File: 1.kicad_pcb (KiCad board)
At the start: 2 copper layers, 55.9 x 35.6 mm, 24 parts, among them J1 Screw_Terminal_01x03, J2 Screw_Terminal_01x01, J3 Screw_Terminal_01x01, U1 LTC2990, U2 LTC2990, U3 LTC2990

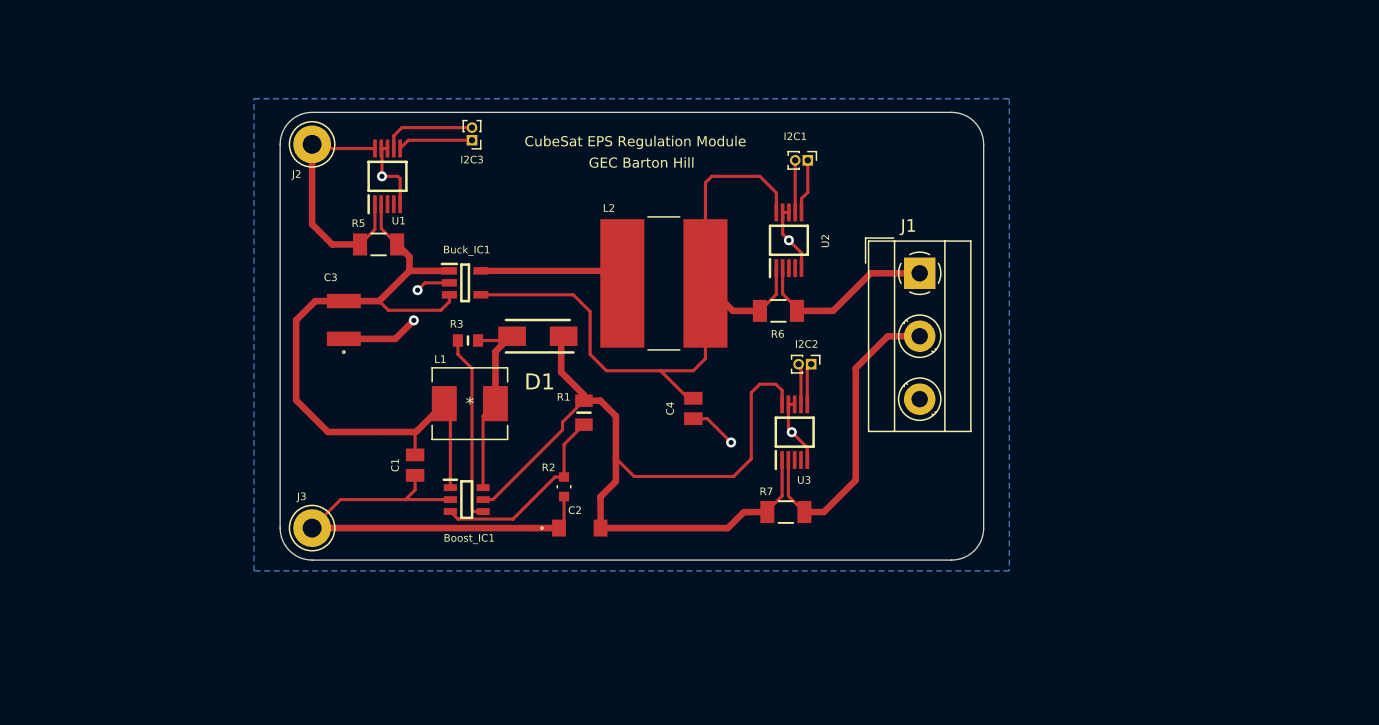
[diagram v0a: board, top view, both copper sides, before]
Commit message: Start redesign coz boost circuit is f'd up
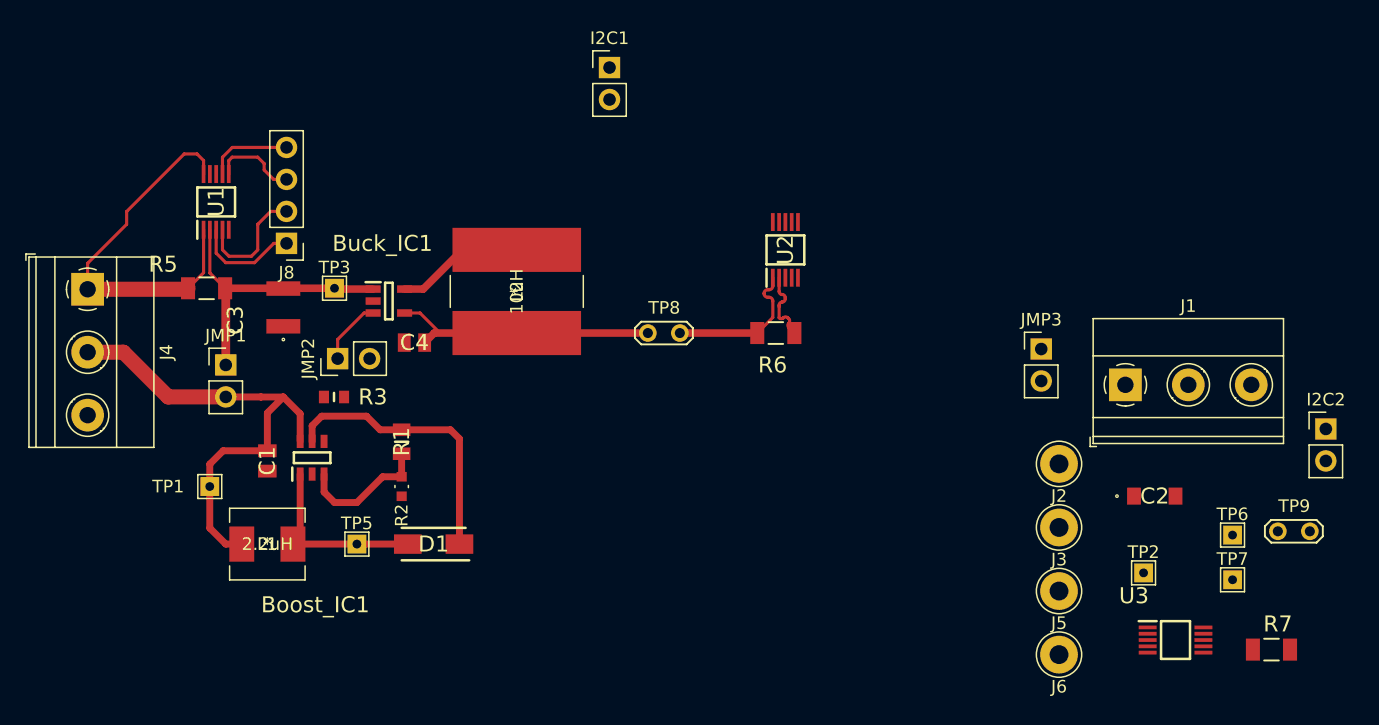
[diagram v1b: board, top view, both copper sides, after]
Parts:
- removed I2C3: EN, Connector_PinHeader_1.00mm:PinHeader_1x02_P1.00mm_Vertical
- added J4: Conn_01x03_Pin, TerminalBlock_Phoenix:TerminalBlock_Phoenix_MKDS-1,5-3_1x03_P5.00mm_Horizontal, F.Cu at (116.8, 82.6)
- added J5: Screw_Terminal_01x01, Connector_Pin:Pin_D1.3mm_L11.0mm_LooseFit, F.Cu at (193.9, 106.6)
- added J6: Screw_Terminal_01x01, Connector_Pin:Pin_D1.3mm_L11.0mm_LooseFit, F.Cu at (193.9, 111.6)
- added J8: Conn_01x04_Pin, Connector_PinHeader_2.54mm:PinHeader_1x04_P2.54mm_Vertical, F.Cu at (132.6, 79.0)
- added JMP1: EN, Connector_PinHeader_2.54mm:PinHeader_1x02_P2.54mm_Vertical, F.Cu at (127.8, 88.6)
- added JMP2: EN, Connector_PinHeader_2.54mm:PinHeader_1x02_P2.54mm_Vertical, F.Cu at (136.6, 88.1)
- added JMP3: EN, Connector_PinHeader_2.54mm:PinHeader_1x02_P2.54mm_Vertical, F.Cu at (192.5, 87.4)
- added TP1: TestPoint, TestPoint:TestPoint_THTPad_1.5x1.5mm_Drill0.7mm, F.Cu at (126.5, 98.3)
- added TP2: TestPoint, TestPoint:TestPoint_THTPad_1.5x1.5mm_Drill0.7mm, F.Cu at (200.7, 105.2)
- added TP3: TestPoint, TestPoint:TestPoint_THTPad_1.5x1.5mm_Drill0.7mm, F.Cu at (136.4, 82.5)
- added TP5: TestPoint, TestPoint:TestPoint_THTPad_1.5x1.5mm_Drill0.7mm, F.Cu at (138.2, 102.9)
- added TP6: TestPoint, TestPoint:TestPoint_THTPad_1.5x1.5mm_Drill0.7mm, F.Cu at (207.7, 102.2)
- added TP7: TestPoint, TestPoint:TestPoint_THTPad_1.5x1.5mm_Drill0.7mm, F.Cu at (207.7, 105.7)
- added TP8: TestPoint_2Pole, TestPoint:TestPoint_2Pads_Pitch2.54mm_Drill0.8mm, F.Cu at (161.3, 86.1)
- added TP9: TestPoint_2Pole, TestPoint:TestPoint_2Pads_Pitch2.54mm_Drill0.8mm, F.Cu at (211.3, 101.9)
- D1: value D_Schottky -> STPS2150A
- I2C1, I2C2: footprint Connector_PinHeader_1.00mm:PinHeader_1x02_P1.00mm_Vertical -> Connector_PinHeader_2.54mm:PinHeader_1x02_P2.54mm_Vertical
- J1: footprint TerminalBlock_MetzConnect:TerminalBlock_MetzConnect_Type055_RT01503HDWU_1x03_P5.00mm_Horizontal -> TerminalBlock_Phoenix:TerminalBlock_Phoenix_MKDS-1,5-3_1x03_P5.00mm_Horizontal
- moved J2 64.5 mm to (193.9, 96.5)
- moved J3 59.3 mm to (193.9, 101.5)
- moved C2 45.7 mm to (201.5, 99.1)
- moved I2C2 41.2 mm to (215.1, 93.7), turned to 0 degrees
- moved R7 40.1 mm to (210.8, 111.3)
- moved U3 34.5 mm to (203.2, 110.5), turned to 0 degrees
- moved C4 22.8 mm to (142.7, 86.9), turned to 180 degrees
- moved L1 19.6 mm to (131.1, 102.9)
- moved J1 18.6 mm to (199.2, 90.2), turned to 0 degrees
- moved D1 18.5 mm to (144.3, 102.9)
- moved I2C1 17.4 mm to (158.2, 65.0), turned to 0 degrees
- moved R1 14.7 mm to (141.7, 94.7)
- moved R5 14.1 mm to (126.2, 82.5)
- moved U1 13.8 mm to (127.0, 75.7)
- moved R2 12.9 mm to (141.7, 98.3)
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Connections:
- Boost_IC1 pad 1: Net-(Boost_IC1-Pad1) -> Net-(Boost_IC1-SW)
- Boost_IC1 pad 5: Net-(Boost_IC1-Pad5) -> Net-(Boost_IC1-VOUT)
- Boost_IC1 pad 6: Net-(Boost_IC1-Pad6) -> Net-(Boost_IC1-VIN)
- Buck_IC1 pad 1: Net-(Boost_IC1-Pad1) -> Net-(Buck_IC1-VI)
- Buck_IC1 pad 3: Net-(Boost_IC1-Pad1) -> Net-(Buck_IC1-EN)
- Buck_IC1 pad 4: Net-(Buck_IC1-Pad4) -> Net-(Buck_IC1-FB)
- C1 pad 1: Net-(Boost_IC1-Pad1) -> Net-(Boost_IC1-VIN)
- C2 pad 2: Net-(Boost_IC1-Pad5) -> Net-(Boost_IC1-VOUT)
- C3 pad 2: Net-(Boost_IC1-Pad1) -> Net-(Buck_IC1-VI)
- C4 pad 1: Net-(Buck_IC1-Pad4) -> Net-(Buck_IC1-FB)
- D1 pad 1: Net-(Boost_IC1-Pad5) -> Net-(Boost_IC1-VOUT)
- D1 pad 2: Net-(Boost_IC1-Pad6) -> Net-(Boost_IC1-SW)
- J2 pad 1: Net-(J2-Pad1) -> Earth
- L1 pad 1: Net-(Boost_IC1-Pad1) -> Net-(Boost_IC1-VIN)
- L1 pad 2: Net-(Boost_IC1-Pad6) -> Net-(Boost_IC1-SW)
- L2 pad 2: Net-(Buck_IC1-Pad4) -> Net-(Buck_IC1-FB)
- R1 pad 2: Net-(Boost_IC1-Pad5) -> Net-(Boost_IC1-VOUT)
- R3 pad 2: Net-(Boost_IC1-Pad6) -> Net-(JMP2-Pin_2)
- R5 pad 1: Net-(J2-Pad1) -> Net-(J4-Pin_1)
- R5 pad 2: Net-(Boost_IC1-Pad1) -> Net-(Buck_IC1-VI)
- R6 pad 1: Net-(Buck_IC1-Pad4) -> Net-(U2-V1)
- R7 pad 1: Net-(Boost_IC1-Pad5) -> Net-(U3-V1)
- U1 pad 1: Net-(J2-Pad1) -> Net-(J4-Pin_1)
- U1 pad 10: Net-(J2-Pad1) -> Net-(J4-Pin_1)
- U1 pad 2: Net-(Boost_IC1-Pad1) -> Net-(Buck_IC1-VI)
- U1 pad 3: unconnected-(U1-Pad3) -> Net-(J8-Pin_1)
- U1 pad 4: unconnected-(U1-Pad4) -> Net-(J8-Pin_2)
- U2 pad 1: Net-(Buck_IC1-Pad4) -> Net-(U2-V1)
- U2 pad 10: Net-(Buck_IC1-Pad4) -> Net-(U2-V1)
- U2 pad 3: unconnected-(U2-Pad3) -> Net-(JMP3-Pin_1)
- U2 pad 4: unconnected-(U2-Pad4) -> Net-(JMP3-Pin_2)
- U3 pad 1: Net-(Boost_IC1-Pad5) -> Net-(U3-V1)
- U3 pad 10: Net-(Boost_IC1-Pad5) -> Net-(U3-V1)
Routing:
- net Net-(Boost_IC1-Pad5): track 69.6 -> 0.00 mm
- net Earth: track 66.5 -> 0.00 mm, vias 6 -> 0
- net Net-(Buck_IC1-Pad4): track 57.3 -> 0.00 mm
- net Net-(Boost_IC1-Pad1): track 55.6 -> 0.00 mm
- net Net-(Boost_IC1-VIN): track 0.00 -> 39.1 mm
- net Net-(J4-Pin_1): track 0.00 -> 30.5 mm
- net Net-(Buck_IC1-FB): track 0.00 -> 27.6 mm
- net Net-(J1-Pin_2): track 24.8 -> 0.00 mm
- net Net-(Buck_IC1-VI): track 0.00 -> 23.2 mm
- net Net-(Boost_IC1-VOUT): track 0.00 -> 22.4 mm
- net Net-(J2-Pad1): track 19.6 -> 0.00 mm
- net Net-(Boost_IC1-Pad6): track 15.8 -> 0.00 mm
- net Net-(Boost_IC1-SW): track 0.00 -> 14.9 mm
- net Net-(Boost_IC1-~{SHDN}): track 14.9 -> 0.00 mm
- net Net-(U2-V1): track 0.00 -> 11.9 mm
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- removed copper zone on B.Cu, net Earth
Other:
- board outline removed
- board text removed: "CubeSat EPS Regulation Module"
- board text removed: "GEC Barton Hill"

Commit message: Almost there
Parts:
- removed I2C1, I2C2, JMP2, JMP3: EN, Connector_PinHeader_2.54mm:PinHeader_1x02_P2.54mm_Vertical
- removed R6, R7: 50m, 50m RST:RESC3216X88N
- removed TP2, TP7: TestPoint, TestPoint:TestPoint_THTPad_1.5x1.5mm_Drill0.7mm
- removed U2, U3: LTC2990, MON & PROTECC:SOP50P490X110-10N
- added J7: Conn_01x01_Pin, Connector_PinHeader_2.54mm:PinHeader_1x01_P2.54mm_Vertical, F.Cu at (136.7, 86.4)
- added J9: Conn_01x01_Pin, Connector_PinHeader_2.54mm:PinHeader_1x01_P2.54mm_Vertical, F.Cu at (138.4, 91.7)
- moved J2 87.7 mm to (113.3, 62.0)
- moved J3 81.8 mm to (112.5, 109.2)
- moved TP6 62.4 mm to (151.4, 75.4)
- moved J6 50.7 mm to (195.8, 61.0)
- moved C2 50.7 mm to (150.9, 101.3), turned to -90 degrees
- moved TP9 50.1 mm to (161.3, 99.8), turned to -90 degrees
- moved J1 28.3 mm to (170.9, 89.8), turned to -90 degrees
- moved R3 4.11 mm to (138.4, 94.7), turned to 0 degrees
- turned TP8 to -90 degrees
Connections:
- TP8 pad 2: Net-(U2-V1) -> Net-(J1-Pin_1)
- TP9 pad 1: Net-(U3-V1) -> Net-(J1-Pin_2)
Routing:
- net Earth: track 0.00 -> 45.0 mm
- net Net-(Boost_IC1-VOUT): track 22.4 -> 44.1 mm
- net Net-(J1-Pin_2): track 0.00 -> 13.2 mm
- net Net-(U2-V1): track 11.9 -> 0.00 mm
- net Net-(J1-Pin_1): track 5.92 -> 10.1 mm
- net Net-(Boost_IC1-~{SHDN}): track 0.00 -> 3.64 mm
- net Net-(J9-Pin_1): track 0.00 -> 3.38 mm
- net Net-(J4-Pin_1): track 30.5 -> 28.4 mm
- net Net-(Buck_IC1-EN): track 5.21 -> 3.88 mm
- added copper zone on F.Cu, net Earth
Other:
- board outline added: 120.1 x 67.1 mm

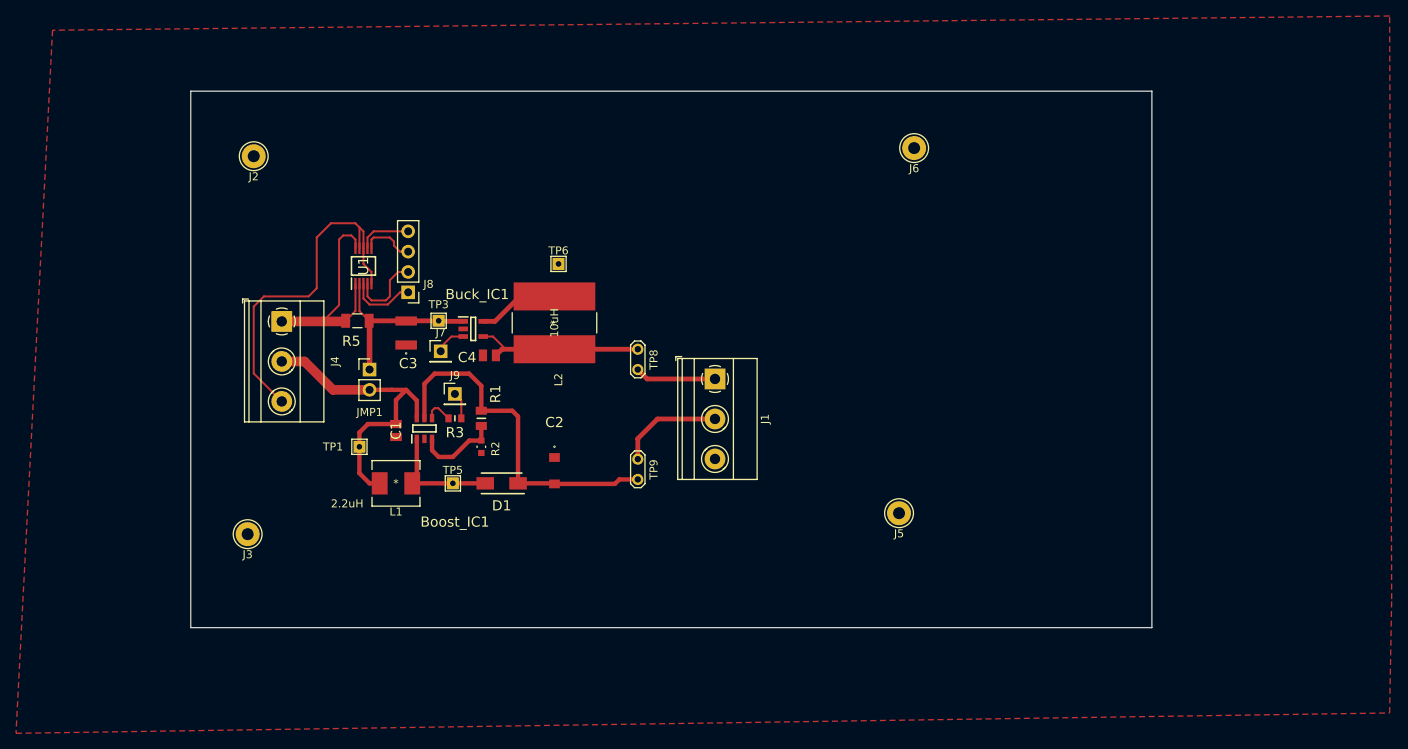
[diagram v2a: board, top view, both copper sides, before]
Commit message: Define edge cuts
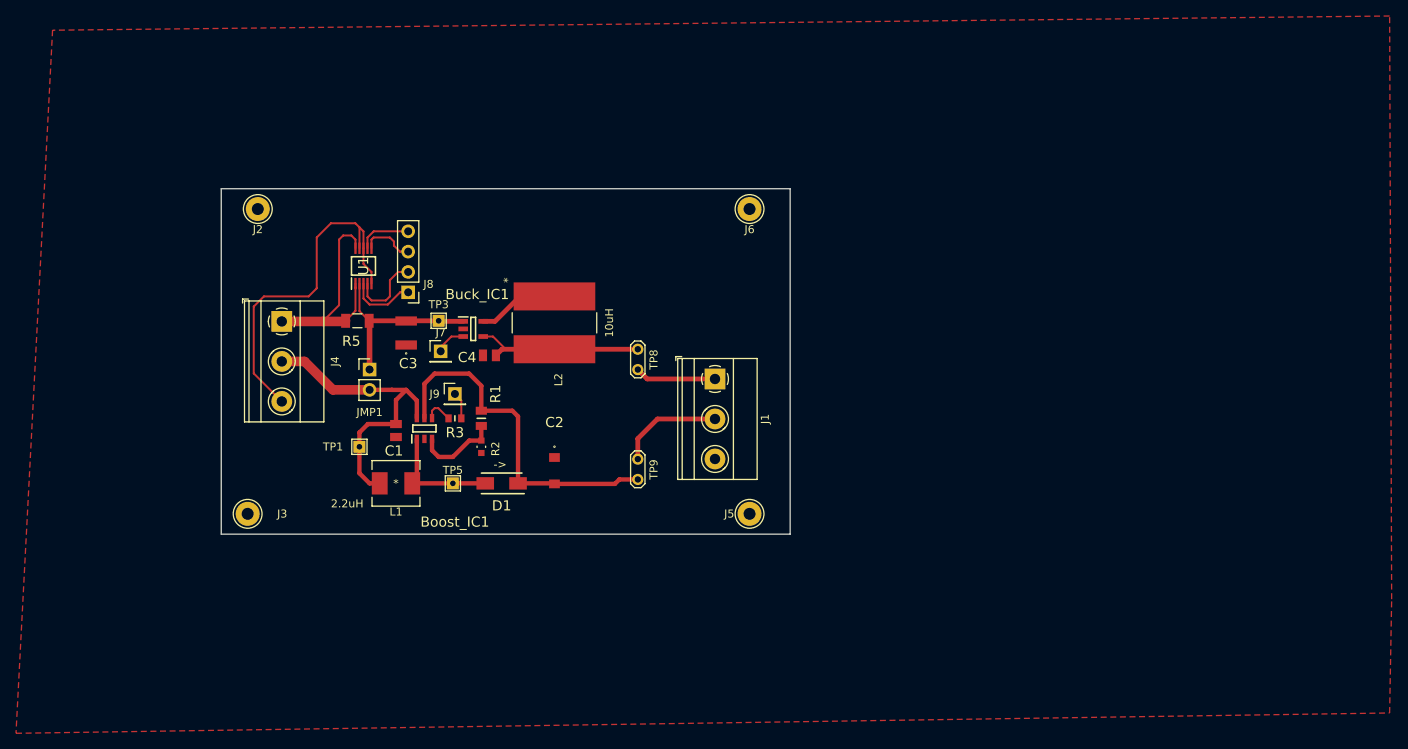
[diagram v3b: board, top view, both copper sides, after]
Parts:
- removed TP6: TestPoint, TestPoint:TestPoint_THTPad_1.5x1.5mm_Drill0.7mm
- moved J6 21.9 mm to (175.3, 68.6)
- moved J5 18.7 mm to (175.3, 106.7)
- moved J2 6.62 mm to (113.8, 68.6)
- moved J3 2.54 mm to (112.5, 106.7)
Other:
- board size 120.1 x 67.1 mm -> 71.1 x 43.2 mm
- board text added: "->"
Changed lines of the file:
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@@
   )
   (footprint "Connector_Pin:Pin_D1.3mm_L11.0mm_LooseFit" (layer "F.Cu")
-    (at 112.522 109.22)
+    (at 112.522 106.68)
     (descr "solder Pin_ diameter 1.3mm, hole diameter 1.5mm (loose fit), length 11.0mm")
     (tags "solder Pin_ loose fit")
@@
     (property "ki_keywords" "screw terminal")
     (attr through_hole)
-    (fp_text reference "J3" (at 0 2.55) (layer "F.SilkS")
+    (fp_text reference "J3" (at 4.318 0) (layer "F.SilkS")
         (effects (font (size 1 1) (thickness 0.15)))
     )
@@
   )
   (footprint "Connector_Pin:Pin_D1.3mm_L11.0mm_LooseFit" (layer "F.Cu")
-    (at 193.946 106.599)
+    (at 175.26 106.68)
     (descr "solder Pin_ diameter 1.3mm, hole diameter 1.5mm (loose fit), length 11.0mm")
     (tags "solder Pin_ loose fit")
@@
     (property "ki_keywords" "screw terminal")
     (attr through_hole)
-    (fp_text reference "J5" (at 0 2.55) (layer "F.SilkS")
+    (fp_text reference "J5" (at -2.54 0) (layer "F.SilkS")
         (effects (font (size 1 1) (thickness 0.15)))
     )
@@
     (property "ki_keywords" "connector")
     (attr through_hole)
-    (fp_text reference "J9" (at 0 -2.33) (layer "F.SilkS")
+    (fp_text reference "J9" (at -2.54 0) (layer "F.SilkS")
         (effects (font (size 1 1) (thickness 0.15)))
     )
@@
       (rotate (xyz 0 0 0))
     )
-  )
-  (footprint "TestPoint:TestPoint_THTPad_1.5x1.5mm_Drill0.7mm" (layer "F.Cu")
-    (at 151.384 75.438)
-    (descr "THT rectangular pad as test Point, square 1.5mm side length, hole diameter 0.7mm")
-    (tags "test point THT pad rectangle square")
-    (property "Sheetfile" "1.kicad_sch")
-    (property "Sheetname" "")
-    (property "ki_description" "test point")
-    (property "ki_keywords" "test point tp")
-    (attr exclude_from_pos_files)
-    (fp_text reference "TP6" (at 0 -1.648) (layer "F.SilkS")
-        (effects (font (size 1 1) (thickness 0.15)))
-    )
-    (fp_text value "TestPoint" (at 0 1.75) (layer "F.Fab")
-        (effects (font (size 1 1) (thickness 0.15)))
-    )
-    (fp_text user "${REFERENCE}" (at 0 -1.65) (layer "F.Fab")
-        (effects (font (size 1 1) (thickness 0.15)))
-    )
-    (fp_line (start -0.95 -0.95) (end 0.95 -0.95)
-      (stroke (width 0.12) (type solid)) (layer "F.SilkS"))
-    (fp_line (start -0.95 0.95) (end -0.95 -0.95)
-      (stroke (width 0.12) (type solid)) (layer "F.SilkS"))
-    (fp_line (start 0.95 -0.95) (end 0.95 0.95)
-      (stroke (width 0.12) (type solid)) (layer "F.SilkS"))
-    (fp_line (start 0.95 0.95) (end -0.95 0.95)
-      (stroke (width 0.12) (type solid)) (layer "F.SilkS"))
-    (fp_line (start -1.25 -1.25) (end -1.25 1.25)
-      (stroke (width 0.05) (type solid)) (layer "F.CrtYd"))
-    (fp_line (start -1.25 -1.25) (end 1.25 -1.25)
-      (stroke (width 0.05) (type solid)) (layer "F.CrtYd"))
-    (fp_line (start 1.25 1.25) (end -1.25 1.25)
-      (stroke (width 0.05) (type solid)) (layer "F.CrtYd"))
-    (fp_line (start 1.25 1.25) (end 1.25 -1.25)
-      (stroke (width 0.05) (type solid)) (layer "F.CrtYd"))
-    (pad "1" thru_hole rect (at 0 0) (size 1.5 1.5) (drill 0.7) (layers "*.Cu" "*.Mask")
-      (net 8 "Net-(Buck_IC1-SW)") (pinfunction "1") (pintype "passive"))
   )
   (footprint "50m RST:RESC3216X88N" (layer "F.Cu")
@@
   )
   (footprint "Connector_Pin:Pin_D1.3mm_L11.0mm_LooseFit" (layer "F.Cu")
-    (at 113.284 61.976)
+    (at 113.792 68.58)
     (descr "solder Pin_ diameter 1.3mm, hole diameter 1.5mm (loose fit), length 11.0mm")
     (tags "solder Pin_ loose fit")
@@
     (property "ki_description" "Cap Aluminum Lytic 10uF 35V 20% (5 X 5.8mm) SMD 0.7 Ohm 160mA 2000h 105C T/R")
     (attr smd)
-    (fp_text reference "C1" (at 0 0 90) (layer "F.SilkS")
+    (fp_text reference "C1" (at 2.54 0.254 -180) (layer "F.SilkS")
         (effects (font (size 1.27 1.27) (thickness 0.254)))
     )
@@
         (effects (font (size 1 1) (thickness 0.15)))
     )
-    (fp_text value "10uH" (at 0 0 90) (layer "F.SilkS")
-        (effects (font (size 1 1) (thickness 0.15)))
-    )
-    (fp_text user "*" (at 0 0 90) (layer "F.SilkS")
+    (fp_text value "10uH" (at 0 -6.858 90) (layer "F.SilkS")
+        (effects (font (size 1 1) (thickness 0.15)))
+    )
+    (fp_text user "*" (at -5.334 5.842 90) (layer "F.SilkS")
         (effects (font (size 1 1) (thickness 0.15)))
     )
@@
   )
   (footprint "Connector_Pin:Pin_D1.3mm_L11.0mm_LooseFit" (layer "F.Cu")
-    (at 195.834 60.96)
+    (at 175.26 68.58)
     (descr "solder Pin_ diameter 1.3mm, hole diameter 1.5mm (loose fit), length 11.0mm")
     (tags "solder Pin_ loose fit")
@@
     )
   )
-  (gr_rect (start 105.41 53.848) (end 225.552 120.904)
+  (gr_rect (start 109.22 66.04) (end 180.34 109.22)
     (stroke (width 0.1) (type default)) (fill none) (layer "Edge.Cuts"))
+  (gr_text "->" (at 143.256 101.092) (layer "F.SilkS")
+    (effects (font (size 1 1) (thickness 0.15)) (justify left bottom))
+  )
+  (gr_text_box "Do not power boost subcircuit under no load"
+    (start 149.352 106.68) (end 155.448 110.236) (layer "F.SilkS")
+      (effects (font (size 0.4 0.4) (thickness 0.1)) (justify top))
+    (stroke (width 0.15) (type solid))  )
   (segment (start 133.096 102.87) (end 138.176 102.87) (width 0.55) (layer "F.Cu") (net 1))
   (segment (start 133.67 102.296) (end 133.096 102.87) (width 0.55) (layer "F.Cu") (net 1))
